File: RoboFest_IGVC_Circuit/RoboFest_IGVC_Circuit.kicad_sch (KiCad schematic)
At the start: 0 parts

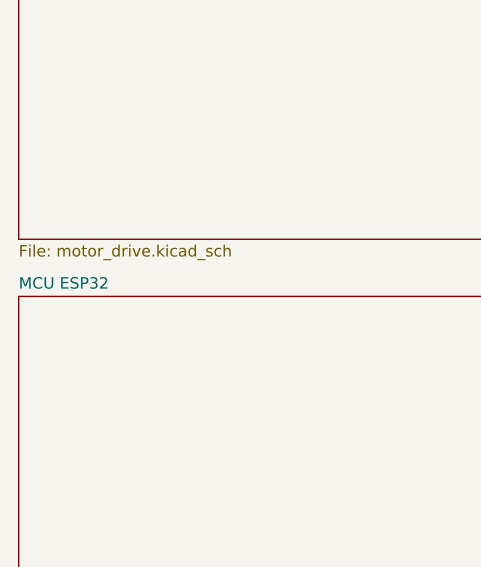
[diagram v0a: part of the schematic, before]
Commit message: added STM32 pinout and report and code
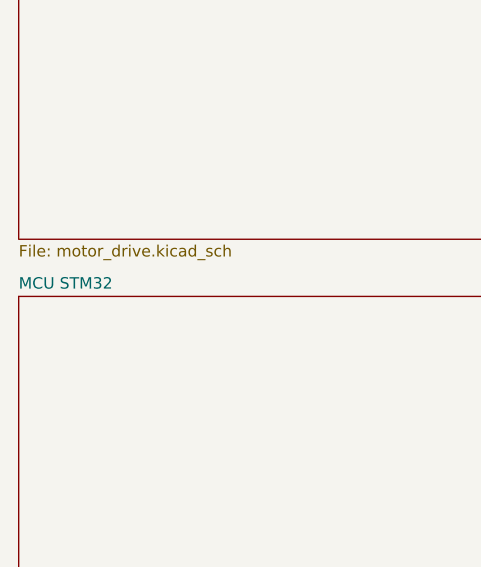
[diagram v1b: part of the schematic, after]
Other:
- sheet MCU ESP32 renamed MCU STM32
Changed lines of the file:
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@@
 			(project "RoboFest_IGVC_Circuit"
 				(path "/bd507979-6024-412b-bdc6-54c3e4be9cc9"
-					(page "5")
+					(page "3")
 				)
 			)
@@
 			(project "RoboFest_IGVC_Circuit"
 				(path "/bd507979-6024-412b-bdc6-54c3e4be9cc9"
-					(page "7")
+					(page "1")
 				)
 			)
@@
 			(project "RoboFest_IGVC_Circuit"
 				(path "/bd507979-6024-412b-bdc6-54c3e4be9cc9"
-					(page "2")
+					(page "6")
 				)
 			)
@@
 			(project "RoboFest_IGVC_Circuit"
 				(path "/bd507979-6024-412b-bdc6-54c3e4be9cc9"
-					(page "4")
+					(page "5")
 				)
 			)
@@
 			(project "RoboFest_IGVC_Circuit"
 				(path "/bd507979-6024-412b-bdc6-54c3e4be9cc9"
-					(page "3")
+					(page "4")
 				)
 			)
@@
 			(color 0 0 0 0)
 		)
-		(property "Sheetname" "MCU ESP32"
+		(property "Sheetname" "MCU STM32"
 			(at 17.78 218.9984 0)
 			(show_name no)
@@
 			(project "RoboFest_IGVC_Circuit"
 				(path "/bd507979-6024-412b-bdc6-54c3e4be9cc9"
-					(page "6")
-				)
-			)
+					(page "2")
+				)
+			)
